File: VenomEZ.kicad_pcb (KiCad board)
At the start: 2 copper layers, 72 x 42 mm, 42 parts, among them CN1 HC-XH-5A-G, CN10 HC-XH-2A-G, CN2 HC-PH-8A-G, CN3 HC-XH-8A-G, CN4 HC-XH-8A-G, CN5 HC-XH-2A-G, CN6 HC-PH-7A-G, CN7 HC-XH-2A-G, CN8 HC-XH-2A-G, CN9 HC-XH-2A-G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

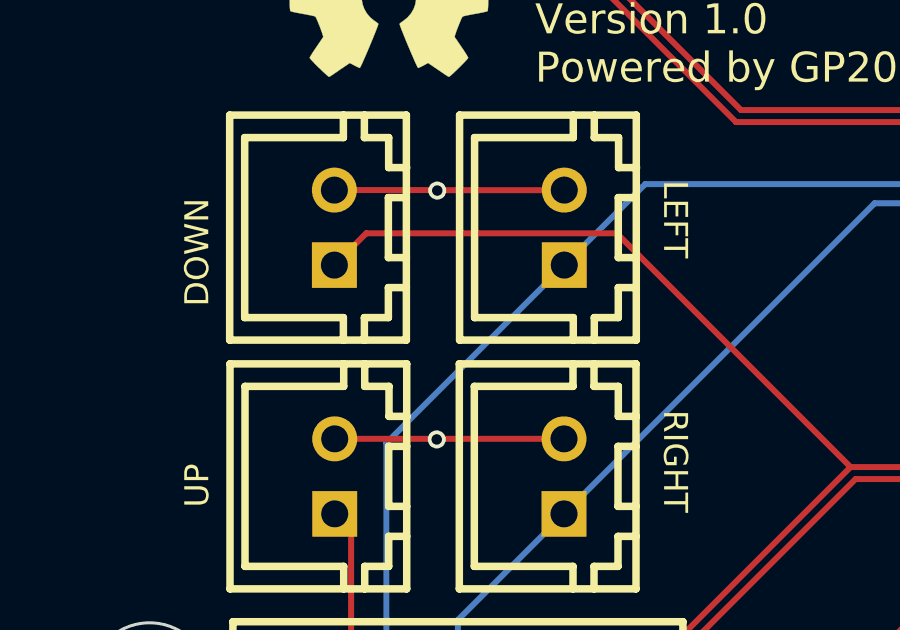
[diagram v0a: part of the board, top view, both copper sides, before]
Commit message: Remove unnecessary ground traces between direction headers
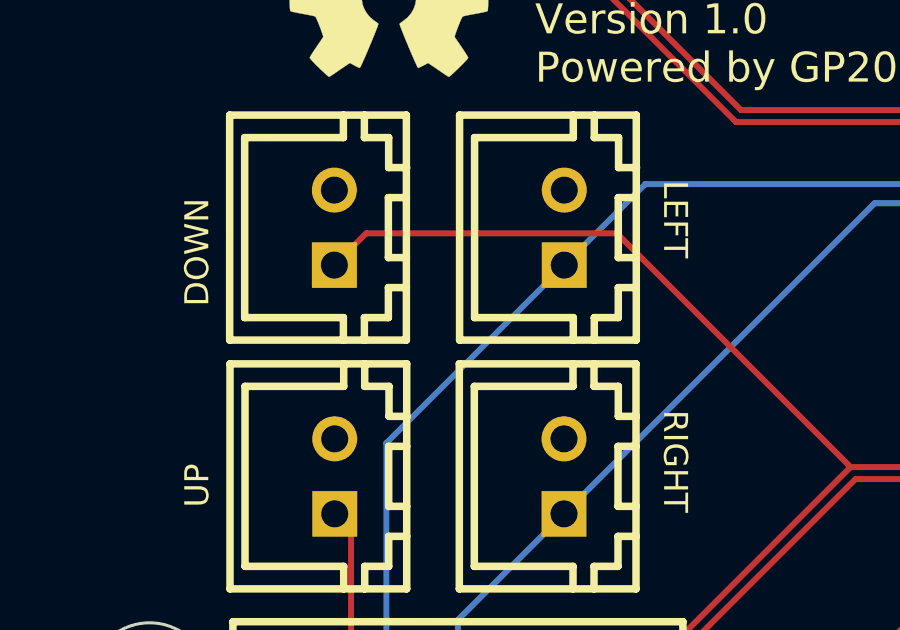
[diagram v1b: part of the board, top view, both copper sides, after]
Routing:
- net GND: track 66.2 -> 50.9 mm, vias 22 -> 20
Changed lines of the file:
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@@
   (segment (start 148.50889 85.458587) (end 148.50889 85.893821) (width 0.2) (layer "F.Cu") (net 2))
   (segment (start 134.980259 86.257429) (end 134.980259 84.41559) (width 0.2) (layer "F.Cu") (net 2))
-  (segment (start 93.135579 94.123747) (end 93.148387 94.110939) (width 0.2) (layer "F.Cu") (net 2))
   (segment (start 115.139266 98.265484) (end 115.094516 98.265484) (width 0.2) (layer "F.Cu") (net 2))
-  (segment (start 93.11963 94.107798) (end 89.706665 94.107798) (width 0.2) (layer "F.Cu") (net 2))
   (segment (start 133.833919 96.52) (end 135.040341 96.52) (width 0.25) (layer "F.Cu") (net 2))
   (segment (start 143.425342 106.058098) (end 144.382096 106.058098) (width 0.2) (layer "F.Cu") (net 2))
@@
   (segment (start 114.3 96.341532) (end 115.507657 95.133875) (width 0.2) (layer "F.Cu") (net 2))
   (segment (start 117.407657 96.833875) (end 117.807657 96.833875) (width 0.2) (layer "F.Cu") (net 2))
-  (segment (start 93.118784 102.418686) (end 93.100236 102.400138) (width 0.2) (layer "F.Cu") (net 2))
-  (segment (start 93.148387 94.110939) (end 97.360856 94.110939) (width 0.2) (layer "F.Cu") (net 2))
   (segment (start 135.220273 103.814592) (end 135.220273 102.932028) (width 0.4) (layer "F.Cu") (net 2))
   (segment (start 129.631769 102.111187) (end 129.631769 103.067779) (width 0.2) (layer "F.Cu") (net 2))
@@
   (segment (start 116.340281 98.265484) (end 115.139266 98.265484) (width 0.2) (layer "F.Cu") (net 2))
   (segment (start 119.763458 97.710662) (end 118.992385 98.481735) (width 0.2) (layer "F.Cu") (net 2))
-  (segment (start 93.100236 102.400138) (end 89.717568 102.400138) (width 0.2) (layer "F.Cu") (net 2))
   (segment (start 125.43422 89.795158) (end 125.43422 88.913282) (width 0.2) (layer "F.Cu") (net 2))
   (segment (start 119.373401 94.531924) (end 119.075352 94.233875) (width 0.2) (layer "F.Cu") (net 2))
@@
   (segment (start 148.519188 90.938016) (end 149.011636 91.430464) (width 0.2) (layer "F.Cu") (net 2))
   (segment (start 114.3 97.426218) (end 114.3 96.341532) (width 0.2) (layer "F.Cu") (net 2))
-  (segment (start 93.135579 94.123747) (end 93.11963 94.107798) (width 0.2) (layer "F.Cu") (net 2))
   (segment (start 115.094516 98.265484) (end 114.3 99.06) (width 0.2) (layer "F.Cu") (net 2))
   (segment (start 139.349548 100.347057) (end 140.21505 100.347057) (width 0.2) (layer "F.Cu") (net 2))
@@
   (segment (start 143.141408 95.713071) (end 144.056408 94.798071) (width 0.4) (layer "F.Cu") (net 2))
   (segment (start 135.220273 102.932028) (end 135.214069 102.925824) (width 0.2) (layer "F.Cu") (net 2))
-  (segment (start 93.137332 102.400138) (end 97.414682 102.400138) (width 0.2) (layer "F.Cu") (net 2))
   (segment (start 129.631769 103.067779) (end 129.624188 103.07536) (width 0.2) (layer "F.Cu") (net 2))
   (segment (start 133.850268 99.678718) (end 135.031036 99.678718) (width 0.25) (layer "F.Cu") (net 2))
@@
   (segment (start 115.507657 95.133875) (end 115.607657 95.133875) (width 0.2) (layer "F.Cu") (net 2))
   (segment (start 115.707657 95.133875) (end 117.407657 96.833875) (width 0.2) (layer "F.Cu") (net 2))
-  (segment (start 93.118784 102.418686) (end 93.137332 102.400138) (width 0.2) (layer "F.Cu") (net 2))
   (segment (start 129.854479 89.375376) (end 129.854479 90.377322) (width 0.4) (layer "F.Cu") (net 2))
   (segment (start 141.519098 95.81) (end 141.217835 95.508737) (width 0.2) (layer "F.Cu") (net 2))
@@
   (via (at 135.044993 96.524652) (size 0.8) (drill 0.4) (layers "F.Cu" "B.Cu") (free) (net 2))
   (via (at 143.425342 106.058098) (size 0.6) (drill 0.35) (layers "F.Cu" "B.Cu") (free) (net 2))
-  (via (at 93.135579 94.123747) (size 0.6) (drill 0.35) (layers "F.Cu" "B.Cu") (free) (net 2))
-  (via (at 93.118784 102.418686) (size 0.6) (drill 0.35) (layers "F.Cu" "B.Cu") (free) (net 2))
   (segment (start 148.182096 107.734963) (end 148.182096 107.558098) (width 0.2) (layer "F.Cu") (net 3))
   (segment (start 112.34482 104.3395) (end 112.54432 104.14) (width 0.2) (layer "F.Cu") (net 3))

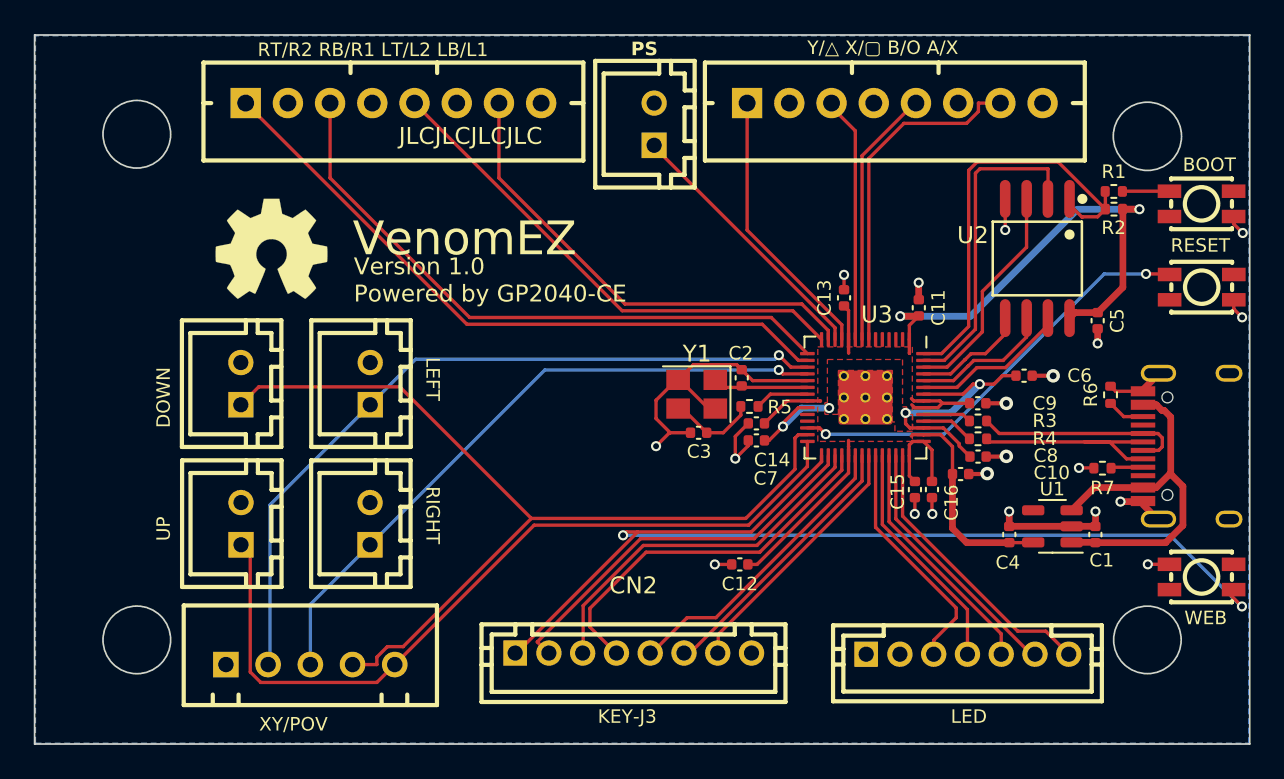
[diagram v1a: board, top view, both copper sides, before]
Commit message: Update some traces for better look
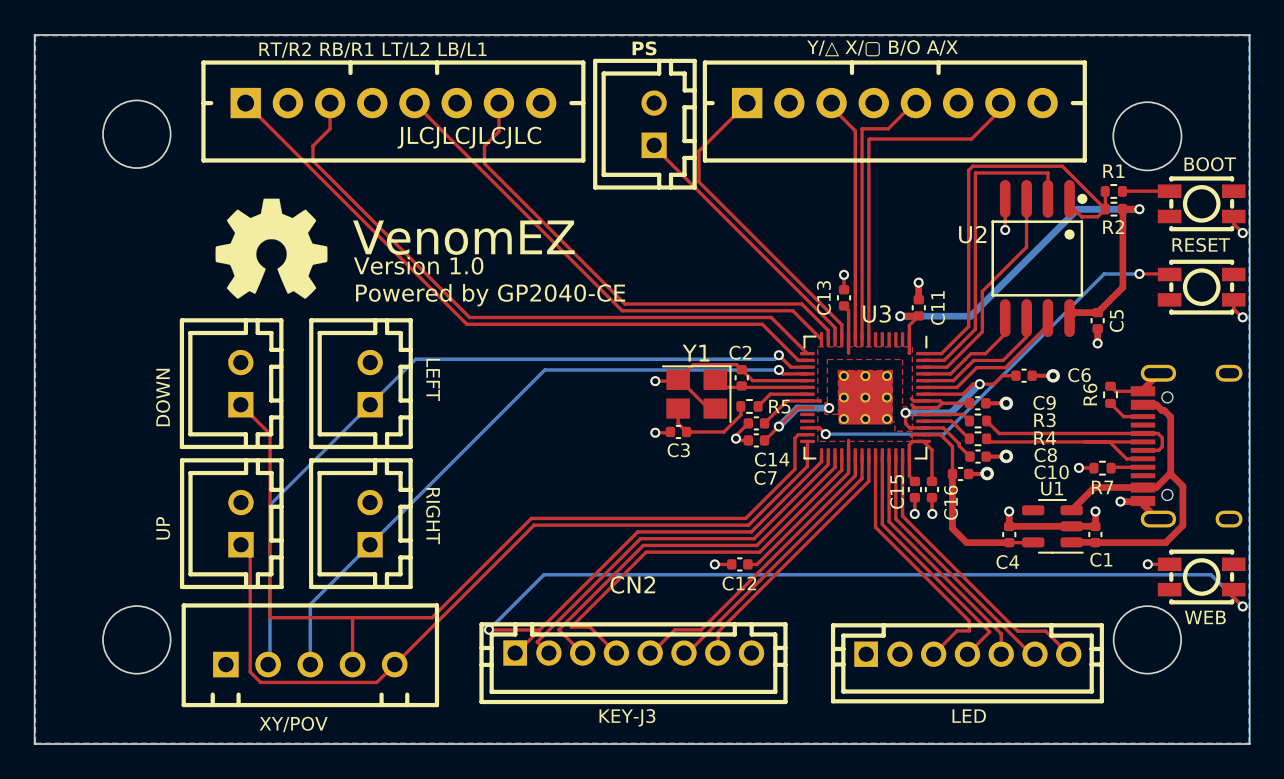
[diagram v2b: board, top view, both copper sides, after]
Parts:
- moved C3 1.19 mm to (115.6, 98.2)
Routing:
- net S2 (START): track 63.9 -> 74.2 mm
- net GND: track 50.9 -> 45.0 mm, vias 20 -> 21
- net (2P) B4: track 16.3 -> 18.7 mm
- net TURBO: track 22.5 -> 24.1 mm
- net DOWN: track 54.8 -> 53.5 mm
- net A2 (TP/CAPTURE): track 21.9 -> 23.1 mm
- net PLED 4: track 13.9 -> 14.9 mm
- net TURBO LED: track 14.3 -> 15.4 mm
- net (2K) B2: track 15.4 -> 16.3 mm
- net (3P) R1: track 37.0 -> 37.9 mm
- net (4P) L1: track 28.2 -> 28.9 mm
- net (1K) B1: track 20.2 -> 20.8 mm

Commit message: Further silk improvements
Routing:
- net (2P) B4: track 18.7 -> 21.7 mm
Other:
- board text added: "Version 1.1 Powered by GP2040-CE"
- board text removed: "Version 1.0 Powered by GP2040-CE"
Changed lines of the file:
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@@
     (effects (font (size 0.8 0.8) (thickness 0.15)) (justify left bottom))
   )
-  (gr_text "Version 1.0\nPowered by GP2040-CE" (at 96.396823 90.614668) (layer "F.SilkS")
+  (gr_text "Version 1.1\nPowered by GP2040-CE" (at 96.396823 90.614668) (layer "F.SilkS")
     (effects (font (size 1 1) (thickness 0.09)) (justify left bottom))
   )
@@
   )
   (segment (start 91.44 98.341133) (end 91.44 109.22) (width 0.2) (layer "F.Cu") (net 1))
+  (segment (start 119.614425 103.34) (end 122.52651 100.427915) (width 0.2) (layer "F.Cu") (net 1))
+  (segment (start 122.52651 100.427915) (end 122.52651 98.585025) (width 0.2) (layer "F.Cu") (net 1))
+  (segment (start 122.52651 98.585025) (end 122.731535 98.38) (width 0.2) (layer "F.Cu") (net 1))
+  (segment (start 89.706665 96.607798) (end 91.44 98.341133) (width 0.2) (layer "F.Cu") (net 1))
   (segment (start 122.731535 98.38) (end 123.26401 98.38) (width 0.2) (layer "F.Cu") (net 1))
-  (segment (start 119.614425 103.34) (end 122.52651 100.427915) (width 0.2) (layer "F.Cu") (net 1))
+  (segment (start 112.884629 103.34) (end 119.614425 103.34) (width 0.2) (layer "F.Cu") (net 1))
   (segment (start 96.296298 109.22) (end 101.033814 109.22) (width 0.2) (layer "F.Cu") (net 1))
-  (segment (start 89.706665 96.607798) (end 91.44 98.341133) (width 0.2) (layer "F.Cu") (net 1))
-  (segment (start 106.913815 103.34) (end 119.614425 103.34) (width 0.2) (layer "F.Cu") (net 1))
-  (segment (start 122.52651 100.427915) (end 122.52651 98.585025) (width 0.2) (layer "F.Cu") (net 1))
   (segment (start 91.44 109.22) (end 96.296298 109.22) (width 0.2) (layer "F.Cu") (net 1))
+  (segment (start 107.292265 108.932363) (end 112.884629 103.34) (width 0.2) (layer "F.Cu") (net 1))
   (segment (start 96.3245 111.995) (end 96.3245 109.248202) (width 0.2) (layer "F.Cu") (net 1))
   (segment (start 96.3245 109.248202) (end 96.296298 109.22) (width 0.2) (layer "F.Cu") (net 1))
-  (segment (start 122.52651 98.585025) (end 122.731535 98.38) (width 0.2) (layer "F.Cu") (net 1))
-  (segment (start 101.033814 109.22) (end 106.913815 103.34) (width 0.2) (layer "F.Cu") (net 1))
+  (segment (start 101.321452 108.932363) (end 107.292265 108.932363) (width 0.2) (layer "F.Cu") (net 1))
+  (segment (start 101.033814 109.22) (end 101.321452 108.932363) (width 0.2) (layer "F.Cu") (net 1))
   (segment (start 130.641428 103.050549) (end 130.666239 103.07536) (width 0.2) (layer "F.Cu") (net 2))
   (segment (start 138.913973 103.807962) (end 140.312251 103.807962) (width 0.4) (layer "F.Cu") (net 2))
@@
   (segment (start 104.14 81.28) (end 104.994448 80.425552) (width 0.2) (layer "F.Cu") (net 21))
   (segment (start 124.50151 92.210025) (end 122.931485 90.64) (width 0.2) (layer "F.Cu") (net 21))
+  (segment (start 123.26401 98.78) (end 123.26401 100.256103) (width 0.2) (layer "F.Cu") (net 22))
   (segment (start 90.2645 105.44707) (end 90.2645 112.434067) (width 0.2) (layer "F.Cu") (net 22))
-  (segment (start 119.780111 103.74) (end 107.07975 103.74) (width 0.2) (layer "F.Cu") (net 22))
   (segment (start 90.885433 113.055) (end 97.7645 113.055) (width 0.2) (layer "F.Cu") (net 22))
+  (segment (start 101.487137 109.332363) (end 98.8245 111.995) (width 0.2) (layer "F.Cu") (net 22))
   (segment (start 97.7645 113.055) (end 98.8245 111.995) (width 0.2) (layer "F.Cu") (net 22))
+  (segment (start 113.050314 103.74) (end 107.457951 109.332363) (width 0.2) (layer "F.Cu") (net 22))
   (segment (start 90.2645 112.434067) (end 90.885433 113.055) (width 0.2) (layer "F.Cu") (net 22))
   (segment (start 89.717568 104.900138) (end 90.2645 105.44707) (width 0.2) (layer "F.Cu") (net 22))
-  (segment (start 107.07975 103.74) (end 98.82475 111.995) (width 0.2) (layer "F.Cu") (net 22))
-  (segment (start 98.82475 111.995) (end 98.8245 111.995) (width 0.2) (layer "F.Cu") (net 22))
-  (segment (start 123.26401 98.78) (end 123.26401 100.256103) (width 0.2) (layer "F.Cu") (net 22))
-  (segment (start 123.26401 100.256103) (end 119.780111 103.74) (width 0.2) (layer "F.Cu") (net 22))
+  (segment (start 123.26401 100.256103) (end 119.780113 103.74) (width 0.2) (layer "F.Cu") (net 22))
+  (segment (start 107.457951 109.332363) (end 101.487137 109.332363) (width 0.2) (layer "F.Cu") (net 22))
+  (segment (start 119.780113 103.74) (end 113.050314 103.74) (width 0.2) (layer "F.Cu") (net 22))
   (segment (start 132.987518 80.869539) (end 134.693878 79.163179) (width 0.2) (layer "F.Cu") (net 23))
   (segment (start 126.90151 92.7425) (end 126.90151 80.910387) (width 0.2) (layer "F.Cu") (net 23))
@@
   (segment (start 124.693878 78.973878) (end 124.693878 78.74) (width 0.2) (layer "F.Cu") (net 25))
   (segment (start 126.10151 80.38151) (end 124.693878 78.973878) (width 0.2) (layer "F.Cu") (net 25))
-  (segment (start 125.30151 91.870485) (end 116.84 83.408975) (width 0.2) (layer "F.Cu") (net 26))
-  (segment (start 116.84 81.593878) (end 119.693878 78.74) (width 0.2) (layer "F.Cu") (net 26))
+  (segment (start 115.899042 82.468017) (end 115.899042 78.74) (width 0.2) (layer "F.Cu") (net 26))
+  (segment (start 125.30151 91.870485) (end 115.899042 82.468017) (width 0.2) (layer "F.Cu") (net 26))
+  (segment (start 115.899042 78.74) (end 119.693878 78.74) (width 0.2) (layer "F.Cu") (net 26))
   (segment (start 125.30151 92.7425) (end 125.30151 91.870485) (width 0.2) (layer "F.Cu") (net 26))
-  (segment (start 116.84 83.408975) (end 116.84 81.593878) (width 0.2) (layer "F.Cu") (net 26))
   (segment (start 123.982048 97.98) (end 124.350536 98.348488) (width 0.2) (layer "F.Cu") (net 30))
   (segment (start 144.686859 88.859795) (end 144.719188 88.892124) (width 0.2) (layer "F.Cu") (net 30))
